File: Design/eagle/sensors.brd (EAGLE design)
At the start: 103 x 33 mm, 10 parts

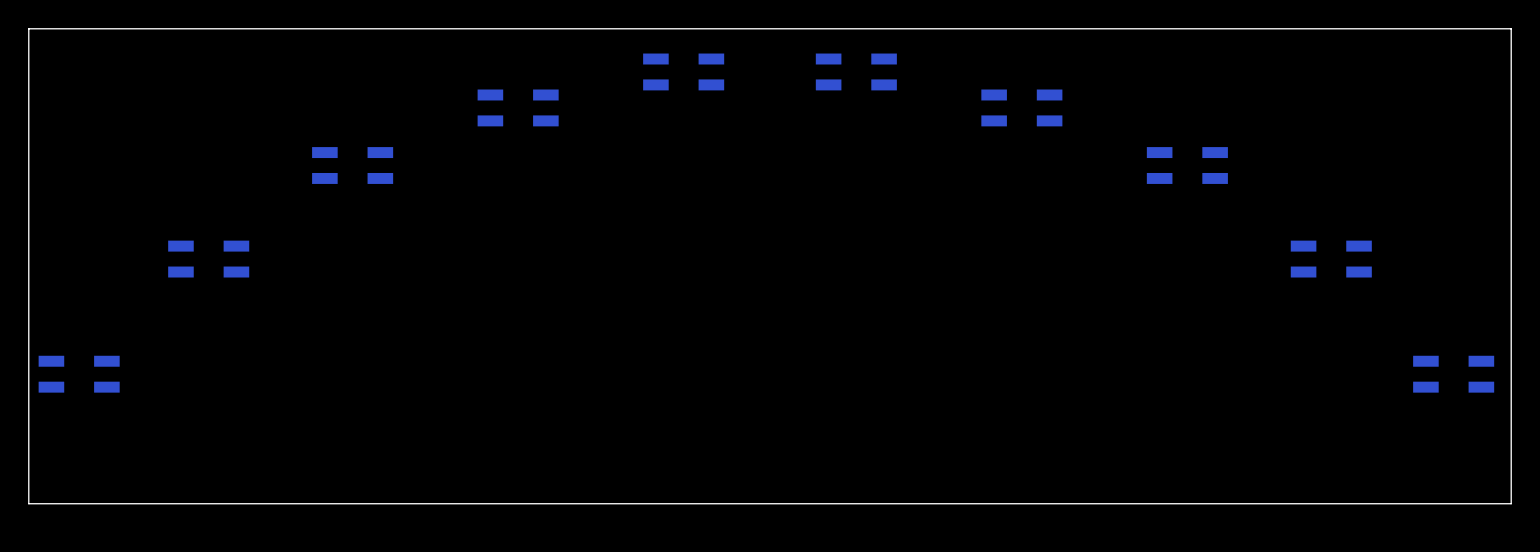
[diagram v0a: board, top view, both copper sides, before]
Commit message: Finished sensor PCB + Analog MUX
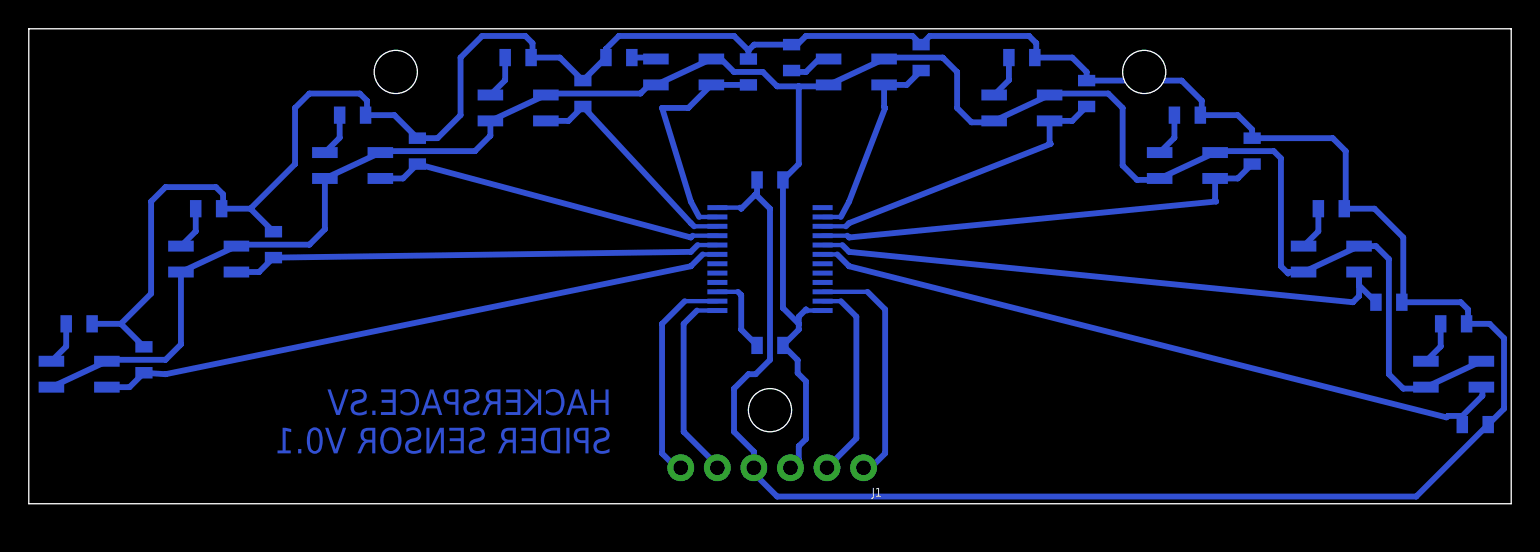
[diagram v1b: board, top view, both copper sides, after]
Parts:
- added C1: 0.1uF, SparkFun-Capacitors:0805
- added IC1: MUX-74HC4067SMD, SeguidorLineasLbr:SSOP24
- added J1: (no value), SparkFun-Connectors:1X06_NO_SILK
- added R1, R10, R11, R12, R13, R14, R15, R16, R17, R18, R19, R2, R20, R3, R4, R5, R6, R7, R8, R9: (no value), SparkFun-Resistors:0805
- added R21: 10K, SparkFun-Resistors:0805
- turned U1 to 180 degrees
- turned U10 to 180 degrees
- turned U2 to 180 degrees
- turned U3 to 180 degrees
- turned U4 to 180 degrees
- turned U5 to 180 degrees
- turned U6 to 180 degrees
- turned U7 to 180 degrees
- turned U8 to 180 degrees
- turned U9 to 180 degrees
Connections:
- new net GND: C1.2, IC1.12, J1.3, R21.2, U1.2, U1.4, U10.2, U10.4, U2.2, U2.4, U3.2, U3.4, U4.2, U4.4, U5.2, U5.4, U6.2, U6.4, U7.2, U7.4, U8.2, U8.4, U9.2, U9.4
- new net N$1: R1.1, U1.1
- new net N$10: IC1.11, J1.2
- new net N$11: R11.1, U6.1
- new net N$13: R13.2, U7.1
- new net N$15: R15.1, U8.1
- new net N$17: R17.1, U9.1
- new net N$19: R19.2, U10.1
- new net N$2: IC1.13, J1.5
- new net N$3: R3.1, U2.1
- new net N$4: IC1.15, R21.1
- new net N$5: R5.2, U3.1
- new net N$6: IC1.14, J1.6
- new net N$7: R7.1, U4.1
- new net N$8: IC1.10, J1.1
- new net N$9: R9.2, U5.1
- new net S10A: IC1.6, R20.2, U10.3
- new net S1A: IC1.19, R2.1, U1.3
- new net S2A: IC1.20, R4.1, U2.3
- new net S3A: IC1.21, R6.2, U3.3
- new net S4A: IC1.22, R8.1, U4.3
- new net S5A: IC1.23, R10.2, U5.3
- new net S6A: IC1.2, R12.1, U6.3
- new net S7A: IC1.3, R14.2, U7.3
- new net S8A: IC1.4, R16.1, U8.3
- new net S9A: IC1.5, R18.1, U9.3
- new net VCC: C1.1, IC1.24, J1.4, R1.2, R10.1, R11.2, R12.2, R13.1, R14.1, R15.2, R16.2, R17.2, R18.2, R19.1, R2.2, R20.1, R3.2, R4.2, R5.1, R6.1, R7.2, R8.2, R9.1
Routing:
- net VCC: track 0.00 -> 233.0 mm
- net GND: track 0.00 -> 172.0 mm
- net S10A: track 0.00 -> 49.3 mm
- net S1A: track 0.00 -> 43.9 mm
- net S9A: track 0.00 -> 42.1 mm
- net S2A: track 0.00 -> 34.0 mm
- net S8A: track 0.00 -> 32.1 mm
- net S3A: track 0.00 -> 24.6 mm
- net S7A: track 0.00 -> 21.6 mm
- net N$8: track 0.00 -> 16.8 mm
- net S4A: track 0.00 -> 16.0 mm
- net S5A: track 0.00 -> 16.0 mm
- net N$6: track 0.00 -> 15.2 mm
- net N$10: track 0.00 -> 14.1 mm
- net S6A: track 0.00 -> 14.1 mm
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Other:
- board text added: "HACKERSPACE.SV SPIDER SENSOR V0.1"

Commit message: Fixed missing COM line from analog MUX
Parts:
- J1: device SparkFun-Connectors:1X06_NO_SILK -> SparkFun-Connectors:1X08_ROUND
- moved C1 2.69 mm to (49.0, 23.5), turned to 90 degrees
- moved J1 2.50 mm to (60.5, 2.50)
- moved R21 2.50 mm to (49.0, 11.0), turned to 0 degrees
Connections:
- new net N$12: IC1.1, J1.5
- net GND: now also J1.4, J1.6; no longer J1.3
- net N$2: now also J1.7; no longer J1.5
- net N$6: now also J1.8; no longer J1.6
- net VCC: now also J1.3; no longer J1.4
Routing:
- net GND: track 172.0 -> 229.1 mm
- net N$12: track 0.00 -> 22.9 mm
- net VCC: track 233.0 -> 235.1 mm, vias 0 -> 2
- net N$2: track 13.7 -> 12.5 mm
- net N$8: track 16.8 -> 15.7 mm
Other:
- board text added: "HACKERSPACE.SV SPIDER EYE SENSOR V0.1"
- board text removed: "HACKERSPACE.SV SPIDER SENSOR V0.1"

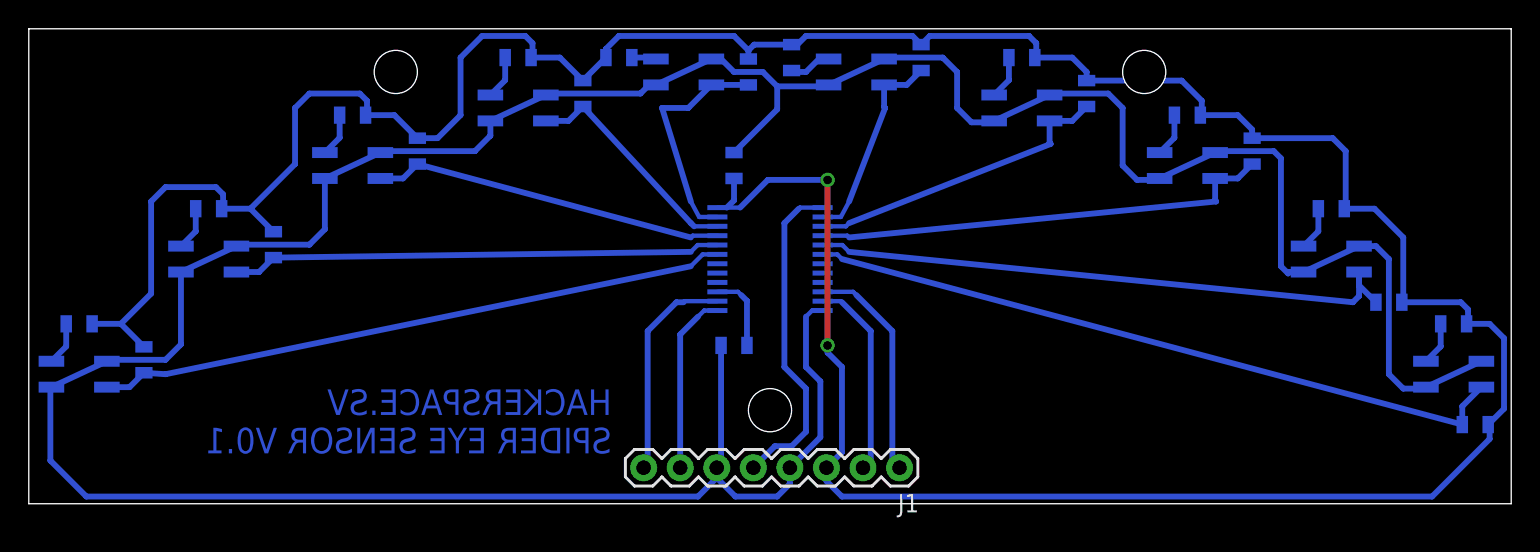
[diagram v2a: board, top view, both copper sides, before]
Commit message: Agregados ajustes en PCB para fotosensibilizada.
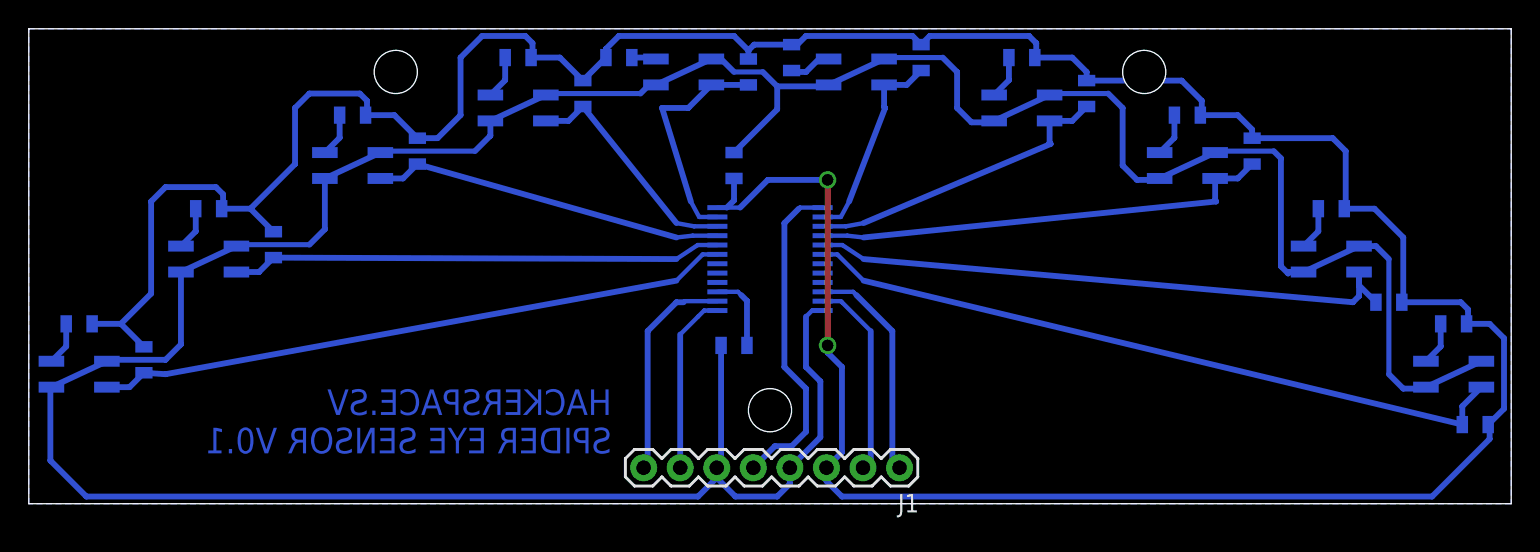
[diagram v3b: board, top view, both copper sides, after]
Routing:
- added copper zone on layer 16, net N$14

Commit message: Agregadas correcciones en PCB
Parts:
- added C2: 10uF, SparkFun-Capacitors:0805
- added R22, R23: 0, SparkFun-Resistors:0805
- R1, R11, R13, R15, R17, R19, R3, R5, R7, R9: value (none) -> 330
- R10, R12, R14, R16, R18, R2, R20, R4, R6, R8: value (none) -> 36K
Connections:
- net GND: now also C2.2
- net VCC: now also C2.1, R22.1, R22.2, R23.1, R23.2
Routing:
- net VCC: track 235.1 -> 228.5 mm, vias 2 -> 0
- net N$10: track 13.9 -> 14.8 mm
